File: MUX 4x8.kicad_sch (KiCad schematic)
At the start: 4 parts, among them U901 74LS253, U902 74LS253, U903 74LS253, U904 74LS253

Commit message: Working
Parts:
- added C1401, C1402, C1403, C1404: C, symbol Device:C
- renumbered U901 to U1403, U902 to U1404, U903 to U1405, U904 to U1406
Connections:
- net +5V: now also C1401.1, C1402.1, C1403.1, C1404.1
- net GND: now also C1401.2, C1402.2, C1403.2, C1404.2

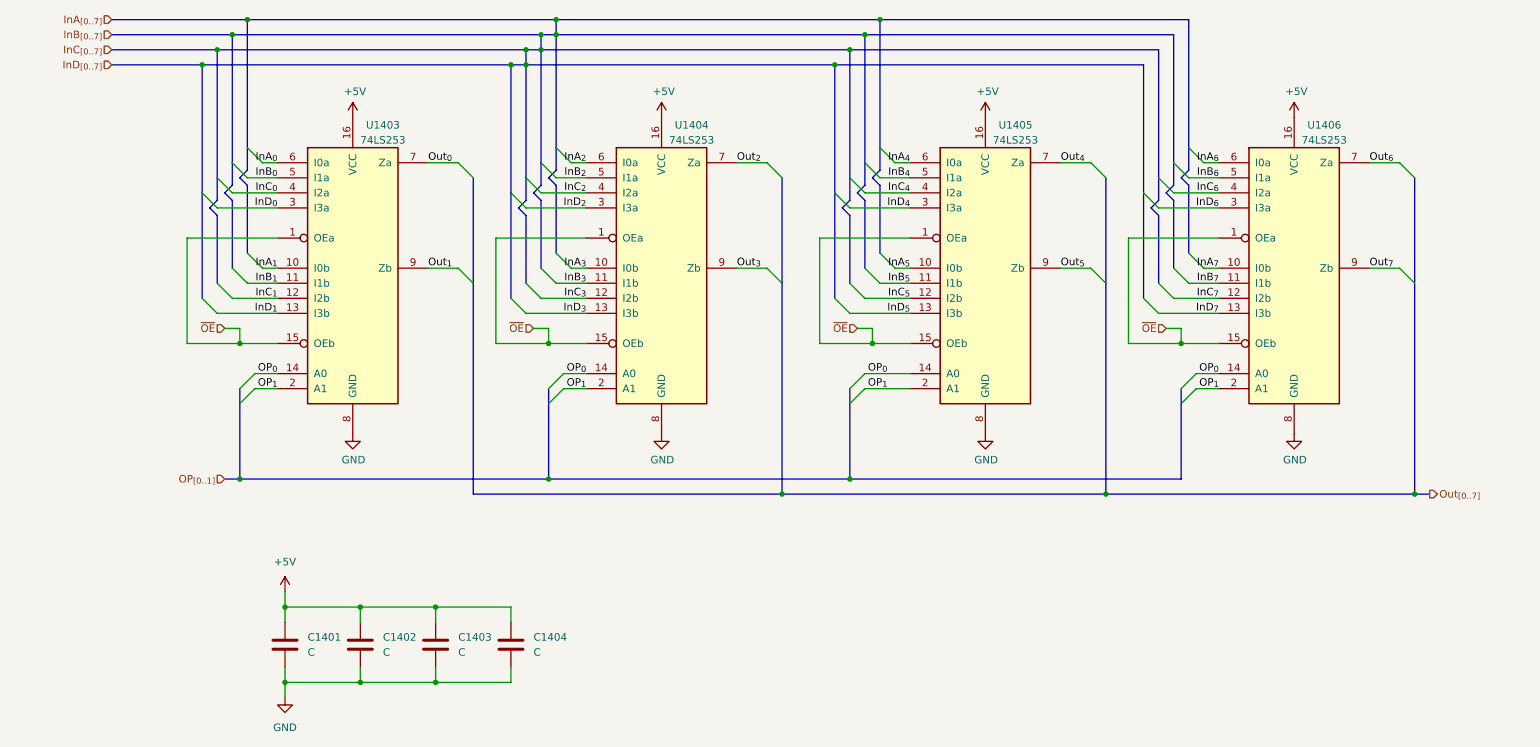
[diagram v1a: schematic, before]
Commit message: More cleanup and preparing signals for control logic
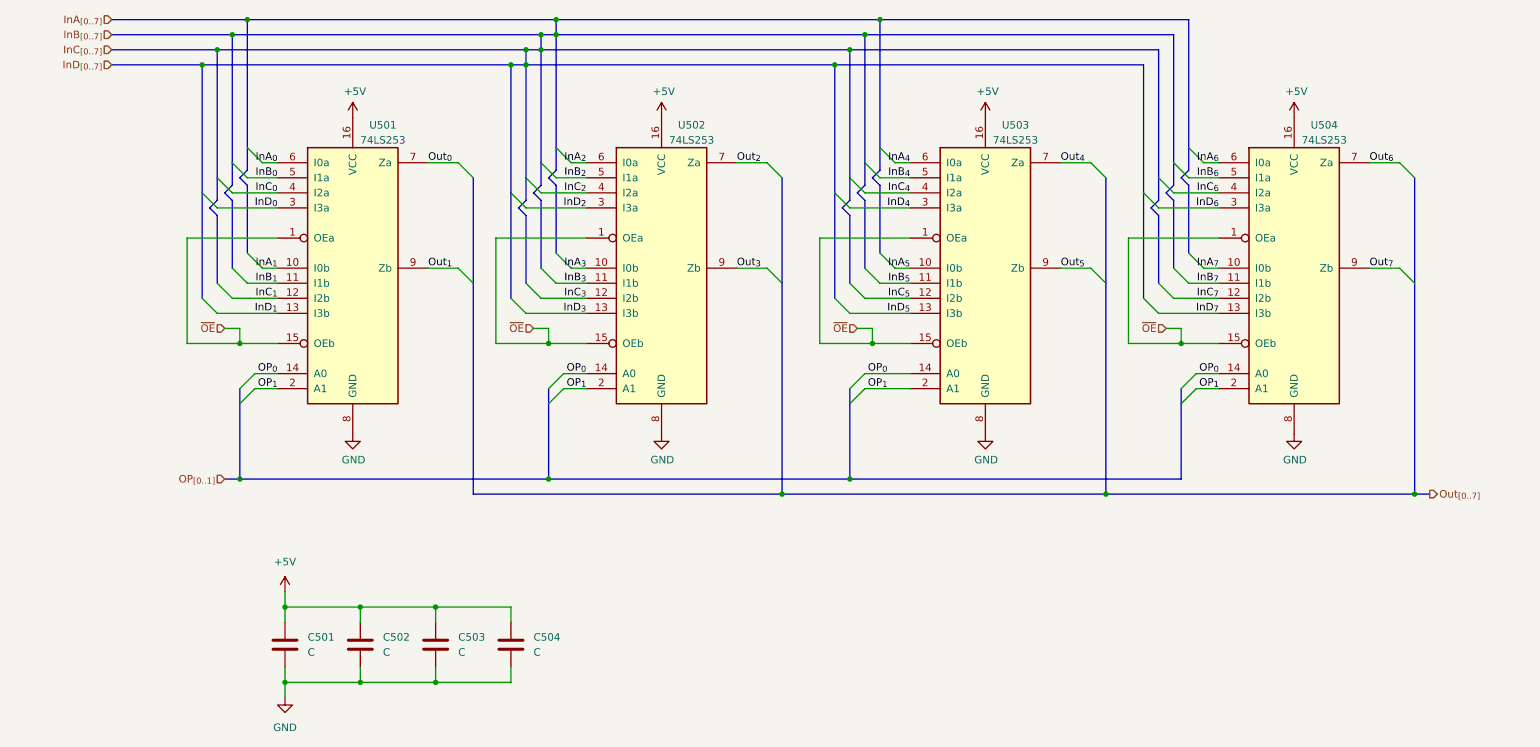
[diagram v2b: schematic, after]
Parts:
- renumbered C1401 to C501, C1402 to C502, C1403 to C503, C1404 to C504, U1403 to U501, U1404 to U502, U1405 to U503, U1406 to U504
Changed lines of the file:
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@@
 		(on_board yes)
 		(dnp no)
-		(property "Reference" "#PWR01405"
+		(property "Reference" "#PWR0504"
 			(at 72.39 107.95 0)
 			(effects
@@
 			(project "BRISC8"
 				(path "/e198223b-f7bd-4b26-ae2e-259db8d07fb6/d081cdcb-1181-4657-9580-dc3ba9a85775/1ff29d81-6c83-4004-b61e-ee24b69c0640/552835a5-6095-4031-9dab-7ccc78242c9c"
-					(reference "#PWR01405")
+					(reference "#PWR0504")
 					(unit 1)
 				)
@@
 		(on_board yes)
 		(dnp no)
-		(property "Reference" "#PWR01401"
+		(property "Reference" "#PWR0503"
 			(at 72.39 52.07 0)
 			(effects
@@
 			(project "BRISC8"
 				(path "/e198223b-f7bd-4b26-ae2e-259db8d07fb6/d081cdcb-1181-4657-9580-dc3ba9a85775/1ff29d81-6c83-4004-b61e-ee24b69c0640/552835a5-6095-4031-9dab-7ccc78242c9c"
-					(reference "#PWR01401")
+					(reference "#PWR0503")
 					(unit 1)
 				)
@@
 		(on_board yes)
 		(dnp no)
-		(property "Reference" "#PWR01406"
+		(property "Reference" "#PWR0506"
 			(at 124.46 107.95 0)
 			(effects
@@
 			(project "BRISC8"
 				(path "/e198223b-f7bd-4b26-ae2e-259db8d07fb6/d081cdcb-1181-4657-9580-dc3ba9a85775/1ff29d81-6c83-4004-b61e-ee24b69c0640/552835a5-6095-4031-9dab-7ccc78242c9c"
-					(reference "#PWR01406")
+					(reference "#PWR0506")
 					(unit 1)
 				)
@@
 		(on_board yes)
 		(dnp no)
-		(property "Reference" "#PWR01402"
+		(property "Reference" "#PWR0505"
 			(at 124.46 52.07 0)
 			(effects
@@
 			(project "BRISC8"
 				(path "/e198223b-f7bd-4b26-ae2e-259db8d07fb6/d081cdcb-1181-4657-9580-dc3ba9a85775/1ff29d81-6c83-4004-b61e-ee24b69c0640/552835a5-6095-4031-9dab-7ccc78242c9c"
-					(reference "#PWR01402")
+					(reference "#PWR0505")
 					(unit 1)
 				)
@@
 		(on_board yes)
 		(dnp no)
-		(property "Reference" "#PWR01407"
+		(property "Reference" "#PWR0508"
 			(at 179.07 107.95 0)
 			(effects
@@
 			(project "BRISC8"
 				(path "/e198223b-f7bd-4b26-ae2e-259db8d07fb6/d081cdcb-1181-4657-9580-dc3ba9a85775/1ff29d81-6c83-4004-b61e-ee24b69c0640/552835a5-6095-4031-9dab-7ccc78242c9c"
-					(reference "#PWR01407")
+					(reference "#PWR0508")
 					(unit 1)
 				)
@@
 		(on_board yes)
 		(dnp no)
-		(property "Reference" "#PWR01403"
+		(property "Reference" "#PWR0507"
 			(at 179.07 52.07 0)
 			(effects
@@
 			(project "BRISC8"
 				(path "/e198223b-f7bd-4b26-ae2e-259db8d07fb6/d081cdcb-1181-4657-9580-dc3ba9a85775/1ff29d81-6c83-4004-b61e-ee24b69c0640/552835a5-6095-4031-9dab-7ccc78242c9c"
-					(reference "#PWR01403")
+					(reference "#PWR0507")
 					(unit 1)
 				)
@@
 		(on_board yes)
 		(dnp no)
-		(property "Reference" "#PWR01408"
+		(property "Reference" "#PWR0510"
 			(at 231.14 107.95 0)
 			(effects
@@
 			(project "BRISC8"
 				(path "/e198223b-f7bd-4b26-ae2e-259db8d07fb6/d081cdcb-1181-4657-9580-dc3ba9a85775/1ff29d81-6c83-4004-b61e-ee24b69c0640/552835a5-6095-4031-9dab-7ccc78242c9c"
-					(reference "#PWR01408")
+					(reference "#PWR0510")
 					(unit 1)
 				)
@@
 		(on_board yes)
 		(dnp no)
-		(property "Reference" "#PWR01404"
+		(property "Reference" "#PWR0509"
 			(at 231.14 52.07 0)
 			(effects
@@
 			(project "BRISC8"
 				(path "/e198223b-f7bd-4b26-ae2e-259db8d07fb6/d081cdcb-1181-4657-9580-dc3ba9a85775/1ff29d81-6c83-4004-b61e-ee24b69c0640/552835a5-6095-4031-9dab-7ccc78242c9c"
-					(reference "#PWR01404")
+					(reference "#PWR0509")
 					(unit 1)
 				)
@@
 		(on_board yes)
 		(dnp no)
-		(property "Reference" "U1403"
+		(property "Reference" "U501"
 			(at 77.47 49.53 0)
 			(effects
@@
 			(project "BRISC8"
 				(path "/e198223b-f7bd-4b26-ae2e-259db8d07fb6/d081cdcb-1181-4657-9580-dc3ba9a85775/1ff29d81-6c83-4004-b61e-ee24b69c0640/552835a5-6095-4031-9dab-7ccc78242c9c"
-					(reference "U1403")
+					(reference "U501")
 					(unit 1)
 				)
@@
 		(on_board yes)
 		(dnp no)
-		(property "Reference" "U1404"
+		(property "Reference" "U502"
 			(at 129.54 49.53 0)
 			(effects
@@
 			(project "BRISC8"
 				(path "/e198223b-f7bd-4b26-ae2e-259db8d07fb6/d081cdcb-1181-4657-9580-dc3ba9a85775/1ff29d81-6c83-4004-b61e-ee24b69c0640/552835a5-6095-4031-9dab-7ccc78242c9c"
-					(reference "U1404")
+					(reference "U502")
 					(unit 1)
 				)
@@
 		(dnp no)
 		(fields_autoplaced yes)
-		(property "Reference" "C1403"
+		(property "Reference" "C503"
 			(at 90.17 135.8899 0)
 			(effects
@@
 			(project "BRISC8"
 				(path "/e198223b-f7bd-4b26-ae2e-259db8d07fb6/d081cdcb-1181-4657-9580-dc3ba9a85775/1ff29d81-6c83-4004-b61e-ee24b69c0640/552835a5-6095-4031-9dab-7ccc78242c9c"
-					(reference "C1403")
+					(reference "C503")
 					(unit 1)
 				)
@@
 		(dnp no)
 		(fields_autoplaced yes)
-		(property "Reference" "C1401"
+		(property "Reference" "C501"
 			(at 64.77 135.8899 0)
 			(effects
@@
 			(project "BRISC8"
 				(path "/e198223b-f7bd-4b26-ae2e-259db8d07fb6/d081cdcb-1181-4657-9580-dc3ba9a85775/1ff29d81-6c83-4004-b61e-ee24b69c0640/552835a5-6095-4031-9dab-7ccc78242c9c"
-					(reference "C1401")
+					(reference "C501")
 					(unit 1)
 				)
@@
 		(on_board yes)
 		(dnp no)
-		(property "Reference" "U1406"
+		(property "Reference" "U504"
 			(at 236.22 49.53 0)
 			(effects
@@
 			(project "BRISC8"
 				(path "/e198223b-f7bd-4b26-ae2e-259db8d07fb6/d081cdcb-1181-4657-9580-dc3ba9a85775/1ff29d81-6c83-4004-b61e-ee24b69c0640/552835a5-6095-4031-9dab-7ccc78242c9c"
-					(reference "U1406")
+					(reference "U504")
 					(unit 1)
 				)
@@
 		(dnp no)
 		(fields_autoplaced yes)
-		(property "Reference" "C1402"
+		(property "Reference" "C502"
 			(at 77.47 135.8899 0)
 			(effects
@@
 			(project "BRISC8"
 				(path "/e198223b-f7bd-4b26-ae2e-259db8d07fb6/d081cdcb-1181-4657-9580-dc3ba9a85775/1ff29d81-6c83-4004-b61e-ee24b69c0640/552835a5-6095-4031-9dab-7ccc78242c9c"
-					(reference "C1402")
+					(reference "C502")
 					(unit 1)
 				)
@@
 		(dnp no)
 		(fields_autoplaced yes)
-		(property "Reference" "C1404"
+		(property "Reference" "C504"
 			(at 102.87 135.8899 0)
 			(effects
@@
 			(project "BRISC8"
 				(path "/e198223b-f7bd-4b26-ae2e-259db8d07fb6/d081cdcb-1181-4657-9580-dc3ba9a85775/1ff29d81-6c83-4004-b61e-ee24b69c0640/552835a5-6095-4031-9dab-7ccc78242c9c"
-					(reference "C1404")
+					(reference "C504")
 					(unit 1)
 				)
@@
 		(dnp no)
 		(fields_autoplaced yes)
-		(property "Reference" "#PWR01410"
+		(property "Reference" "#PWR0502"
 			(at 60.96 152.4 0)
 			(effects
@@
 			(project "BRISC8"
 				(path "/e198223b-f7bd-4b26-ae2e-259db8d07fb6/d081cdcb-1181-4657-9580-dc3ba9a85775/1ff29d81-6c83-4004-b61e-ee24b69c0640/552835a5-6095-4031-9dab-7ccc78242c9c"
-					(reference "#PWR01410")
+					(reference "#PWR0502")
 					(unit 1)
 				)
@@
 		(on_board yes)
 		(dnp no)
-		(property "Reference" "U1405"
+		(property "Reference" "U503"
 			(at 184.15 49.53 0)
 			(effects
@@
 			(project "BRISC8"
 				(path "/e198223b-f7bd-4b26-ae2e-259db8d07fb6/d081cdcb-1181-4657-9580-dc3ba9a85775/1ff29d81-6c83-4004-b61e-ee24b69c0640/552835a5-6095-4031-9dab-7ccc78242c9c"
-					(reference "U1405")
+					(reference "U503")
 					(unit 1)
 				)
@@
 		(dnp no)
 		(fields_autoplaced yes)
-		(property "Reference" "#PWR01409"
+		(property "Reference" "#PWR0501"
 			(at 60.96 132.08 0)
 			(effects
@@
 			(project "BRISC8"
 				(path "/e198223b-f7bd-4b26-ae2e-259db8d07fb6/d081cdcb-1181-4657-9580-dc3ba9a85775/1ff29d81-6c83-4004-b61e-ee24b69c0640/552835a5-6095-4031-9dab-7ccc78242c9c"
-					(reference "#PWR01409")
-					(unit 1)
-				)
+					(reference "#PWR0501")
+					(unit 1)
+				)

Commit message: Fixed(?)
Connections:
- net InB_{0} renamed AND_{0}
- net InB_{1} renamed AND_{1}
- net InB_{2} renamed AND_{2}
- net InB_{3} renamed AND_{3}
- net InB_{4} renamed AND_{4}
- net InB_{5} renamed AND_{5}
- net InB_{6} renamed AND_{6}
- net InB_{7} renamed AND_{7}
- net InC_{0} renamed XOR_{0}
- net InC_{1} renamed XOR_{1}
- net InC_{2} renamed XOR_{2}
- net InC_{3} renamed XOR_{3}
- net InC_{4} renamed XOR_{4}
- net InC_{5} renamed XOR_{5}
- net InC_{6} renamed XOR_{6}
- net InC_{7} renamed XOR_{7}
- net InD_{0} renamed ADD_{0}
- net InD_{1} renamed ADD_{1}
- net InD_{2} renamed ADD_{2}
- net InD_{3} renamed ADD_{3}
- net InD_{4} renamed ADD_{4}
- net InD_{5} renamed ADD_{5}
- net InD_{6} renamed ADD_{6}
- net InD_{7} renamed ADD_{7}

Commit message: Fixed better
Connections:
- net ADD_{0} renamed InD_{0}
- net ADD_{1} renamed InD_{1}
- net ADD_{2} renamed InD_{2}
- net ADD_{3} renamed InD_{3}
- net ADD_{4} renamed InD_{4}
- net ADD_{5} renamed InD_{5}
- net ADD_{6} renamed InD_{6}
- net ADD_{7} renamed InD_{7}
- net AND_{0} renamed InB_{0}
- net AND_{1} renamed InB_{1}
- net AND_{2} renamed InB_{2}
- net AND_{3} renamed InB_{3}
- net AND_{4} renamed InB_{4}
- net AND_{5} renamed InB_{5}
- net AND_{6} renamed InB_{6}
- net AND_{7} renamed InB_{7}
- net XOR_{0} renamed InC_{0}
- net XOR_{1} renamed InC_{1}
- net XOR_{2} renamed InC_{2}
- net XOR_{3} renamed InC_{3}
- net XOR_{4} renamed InC_{4}
- net XOR_{5} renamed InC_{5}
- net XOR_{6} renamed InC_{6}
- net XOR_{7} renamed InC_{7}

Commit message: Draft Schematic
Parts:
- C501, C502, C503, C504: value C -> 0.1uF; footprint (none) -> Capacitor_THT:C_Rect_L4.0mm_W2.5mm_P2.50mm
- U501, U502, U503, U504: value 74LS253 -> 74HC253; footprint (none) -> Package_DIP:DIP-16_W7.62mm
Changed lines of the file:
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@@
 	(title_block
 		(title "BRISC8 CPU")
-		(date "2025-06-05")
+		(date "2025-06-26")
 		(rev "v1.0.0")
 		(company "Brian Duffy")
@@
 		(on_board yes)
 		(dnp no)
-		(property "Reference" "#PWR0504"
+		(property "Reference" "#PWR0505"
 			(at 72.39 107.95 0)
 			(effects
@@
 			(project "BRISC8"
 				(path "/e198223b-f7bd-4b26-ae2e-259db8d07fb6/d081cdcb-1181-4657-9580-dc3ba9a85775/1ff29d81-6c83-4004-b61e-ee24b69c0640/552835a5-6095-4031-9dab-7ccc78242c9c"
-					(reference "#PWR0504")
+					(reference "#PWR0505")
 					(unit 1)
 				)
@@
 		(on_board yes)
 		(dnp no)
-		(property "Reference" "#PWR0503"
+		(property "Reference" "#PWR0501"
 			(at 72.39 52.07 0)
 			(effects
@@
 			(project "BRISC8"
 				(path "/e198223b-f7bd-4b26-ae2e-259db8d07fb6/d081cdcb-1181-4657-9580-dc3ba9a85775/1ff29d81-6c83-4004-b61e-ee24b69c0640/552835a5-6095-4031-9dab-7ccc78242c9c"
-					(reference "#PWR0503")
+					(reference "#PWR0501")
 					(unit 1)
 				)
@@
 		(on_board yes)
 		(dnp no)
-		(property "Reference" "#PWR0505"
+		(property "Reference" "#PWR0502"
 			(at 124.46 52.07 0)
 			(effects
@@
 			(project "BRISC8"
 				(path "/e198223b-f7bd-4b26-ae2e-259db8d07fb6/d081cdcb-1181-4657-9580-dc3ba9a85775/1ff29d81-6c83-4004-b61e-ee24b69c0640/552835a5-6095-4031-9dab-7ccc78242c9c"
-					(reference "#PWR0505")
+					(reference "#PWR0502")
 					(unit 1)
 				)
@@
 		(on_board yes)
 		(dnp no)
-		(property "Reference" "#PWR0508"
+		(property "Reference" "#PWR0507"
 			(at 179.07 107.95 0)
 			(effects
@@
 			(project "BRISC8"
 				(path "/e198223b-f7bd-4b26-ae2e-259db8d07fb6/d081cdcb-1181-4657-9580-dc3ba9a85775/1ff29d81-6c83-4004-b61e-ee24b69c0640/552835a5-6095-4031-9dab-7ccc78242c9c"
-					(reference "#PWR0508")
+					(reference "#PWR0507")
 					(unit 1)
 				)
@@
 		(on_board yes)
 		(dnp no)
-		(property "Reference" "#PWR0507"
+		(property "Reference" "#PWR0503"
 			(at 179.07 52.07 0)
 			(effects
@@
 			(project "BRISC8"
 				(path "/e198223b-f7bd-4b26-ae2e-259db8d07fb6/d081cdcb-1181-4657-9580-dc3ba9a85775/1ff29d81-6c83-4004-b61e-ee24b69c0640/552835a5-6095-4031-9dab-7ccc78242c9c"
-					(reference "#PWR0507")
+					(reference "#PWR0503")
 					(unit 1)
 				)
@@
 		(on_board yes)
 		(dnp no)
-		(property "Reference" "#PWR0510"
+		(property "Reference" "#PWR0508"
 			(at 231.14 107.95 0)
 			(effects
@@
 			(project "BRISC8"
 				(path "/e198223b-f7bd-4b26-ae2e-259db8d07fb6/d081cdcb-1181-4657-9580-dc3ba9a85775/1ff29d81-6c83-4004-b61e-ee24b69c0640/552835a5-6095-4031-9dab-7ccc78242c9c"
-					(reference "#PWR0510")
+					(reference "#PWR0508")
 					(unit 1)
 				)
@@
 		(on_board yes)
 		(dnp no)
-		(property "Reference" "#PWR0509"
+		(property "Reference" "#PWR0504"
 			(at 231.14 52.07 0)
 			(effects
@@
 			(project "BRISC8"
 				(path "/e198223b-f7bd-4b26-ae2e-259db8d07fb6/d081cdcb-1181-4657-9580-dc3ba9a85775/1ff29d81-6c83-4004-b61e-ee24b69c0640/552835a5-6095-4031-9dab-7ccc78242c9c"
-					(reference "#PWR0509")
+					(reference "#PWR0504")
 					(unit 1)
 				)
@@
 			)
 		)
-		(property "Value" "74LS253"
+		(property "Value" "74HC253"
 			(at 77.47 52.07 0)
 			(effects
@@
 			)
 		)
-		(property "Footprint" ""
+		(property "Footprint" "Package_DIP:DIP-16_W7.62mm"
 			(at 72.39 73.66 0)
 			(effects
@@
 			)
 		)
-		(property "Value" "74LS253"
+		(property "Value" "74HC253"
 			(at 129.54 52.07 0)
 			(effects
@@
 			)
 		)
-		(property "Footprint" ""
+		(property "Footprint" "Package_DIP:DIP-16_W7.62mm"
 			(at 124.46 73.66 0)
 			(effects
@@
 			)
 		)
-		(property "Value" "C"
+		(property "Value" "0.1uF"
 			(at 90.17 138.4299 0)
 			(effects
@@
 			)
 		)
-		(property "Footprint" ""
+		(property "Footprint" "Capacitor_THT:C_Rect_L4.0mm_W2.5mm_P2.50mm"
 			(at 87.3252 140.97 0)
 			(effects
@@
 			)
 		)
-		(property "Value" "C"
+		(property "Value" "0.1uF"
 			(at 64.77 138.4299 0)
 			(effects
@@
 			)
 		)
-		(property "Footprint" ""
+		(property "Footprint" "Capacitor_THT:C_Rect_L4.0mm_W2.5mm_P2.50mm"
 			(at 61.9252 140.97 0)
 			(effects
@@
 			)
 		)
-		(property "Value" "74LS253"
+		(property "Value" "74HC253"
 			(at 236.22 52.07 0)
 			(effects
@@
 			)
 		)
-		(property "Footprint" ""
+		(property "Footprint" "Package_DIP:DIP-16_W7.62mm"
 			(at 231.14 73.66 0)
 			(effects
@@
 			)
 		)
-		(property "Value" "C"
+		(property "Value" "0.1uF"
 			(at 77.47 138.4299 0)
 			(effects
@@
 			)
 		)
-		(property "Footprint" ""
+		(property "Footprint" "Capacitor_THT:C_Rect_L4.0mm_W2.5mm_P2.50mm"
 			(at 74.6252 140.97 0)
 			(effects
@@
 			)
 		)
-		(property "Value" "C"
+		(property "Value" "0.1uF"
 			(at 102.87 138.4299 0)
 			(effects
@@
 			)
 		)
-		(property "Footprint" ""
+		(property "Footprint" "Capacitor_THT:C_Rect_L4.0mm_W2.5mm_P2.50mm"
 			(at 100.0252 140.97 0)
 			(effects
@@
 		(dnp no)
 		(fields_autoplaced yes)
-		(property "Reference" "#PWR0502"
+		(property "Reference" "#PWR0510"
 			(at 60.96 152.4 0)
 			(effects
@@
 			(project "BRISC8"
 				(path "/e198223b-f7bd-4b26-ae2e-259db8d07fb6/d081cdcb-1181-4657-9580-dc3ba9a85775/1ff29d81-6c83-4004-b61e-ee24b69c0640/552835a5-6095-4031-9dab-7ccc78242c9c"
-					(reference "#PWR0502")
+					(reference "#PWR0510")
 					(unit 1)
 				)
@@
 			)
 		)
-		(property "Value" "74LS253"
+		(property "Value" "74HC253"
 			(at 184.15 52.07 0)
 			(effects
@@
 			)
 		)
-		(property "Footprint" ""
+		(property "Footprint" "Package_DIP:DIP-16_W7.62mm"
 			(at 179.07 73.66 0)
 			(effects
@@
 		(dnp no)
 		(fields_autoplaced yes)
-		(property "Reference" "#PWR0501"
+		(property "Reference" "#PWR0509"
 			(at 60.96 132.08 0)
 			(effects
@@
 			(project "BRISC8"
 				(path "/e198223b-f7bd-4b26-ae2e-259db8d07fb6/d081cdcb-1181-4657-9580-dc3ba9a85775/1ff29d81-6c83-4004-b61e-ee24b69c0640/552835a5-6095-4031-9dab-7ccc78242c9c"
-					(reference "#PWR0501")
+					(reference "#PWR0509")
 					(unit 1)
 				)
